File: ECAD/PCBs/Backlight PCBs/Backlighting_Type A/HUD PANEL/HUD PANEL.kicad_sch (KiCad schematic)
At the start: 64 parts, among them J1 Conn_01x04_Female, J2 Conn_01x04_Female

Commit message: Drawing Sheet & Silkscreen update - Backlight Panels (Fc thru Spin)
1:  Updated/Relinked Drawing Sheet for both PCB and Schematics
2:  Standardized Silkscreen (if required)

Finished Remaining Backlighting Type A & Type B PCBs.....
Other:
- title: (none) -> HUD PANEL
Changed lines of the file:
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@@
 (kicad_sch (version 20211123) (generator eeschema)
   (paper "A4")
+  (title_block
+    (title "HUD PANEL")
+    (date "2023-02-10")
+    (rev "3")
+  )
   (junction (at 64.77 133.35) (diameter 0) (color 0 0 0 0)
   )

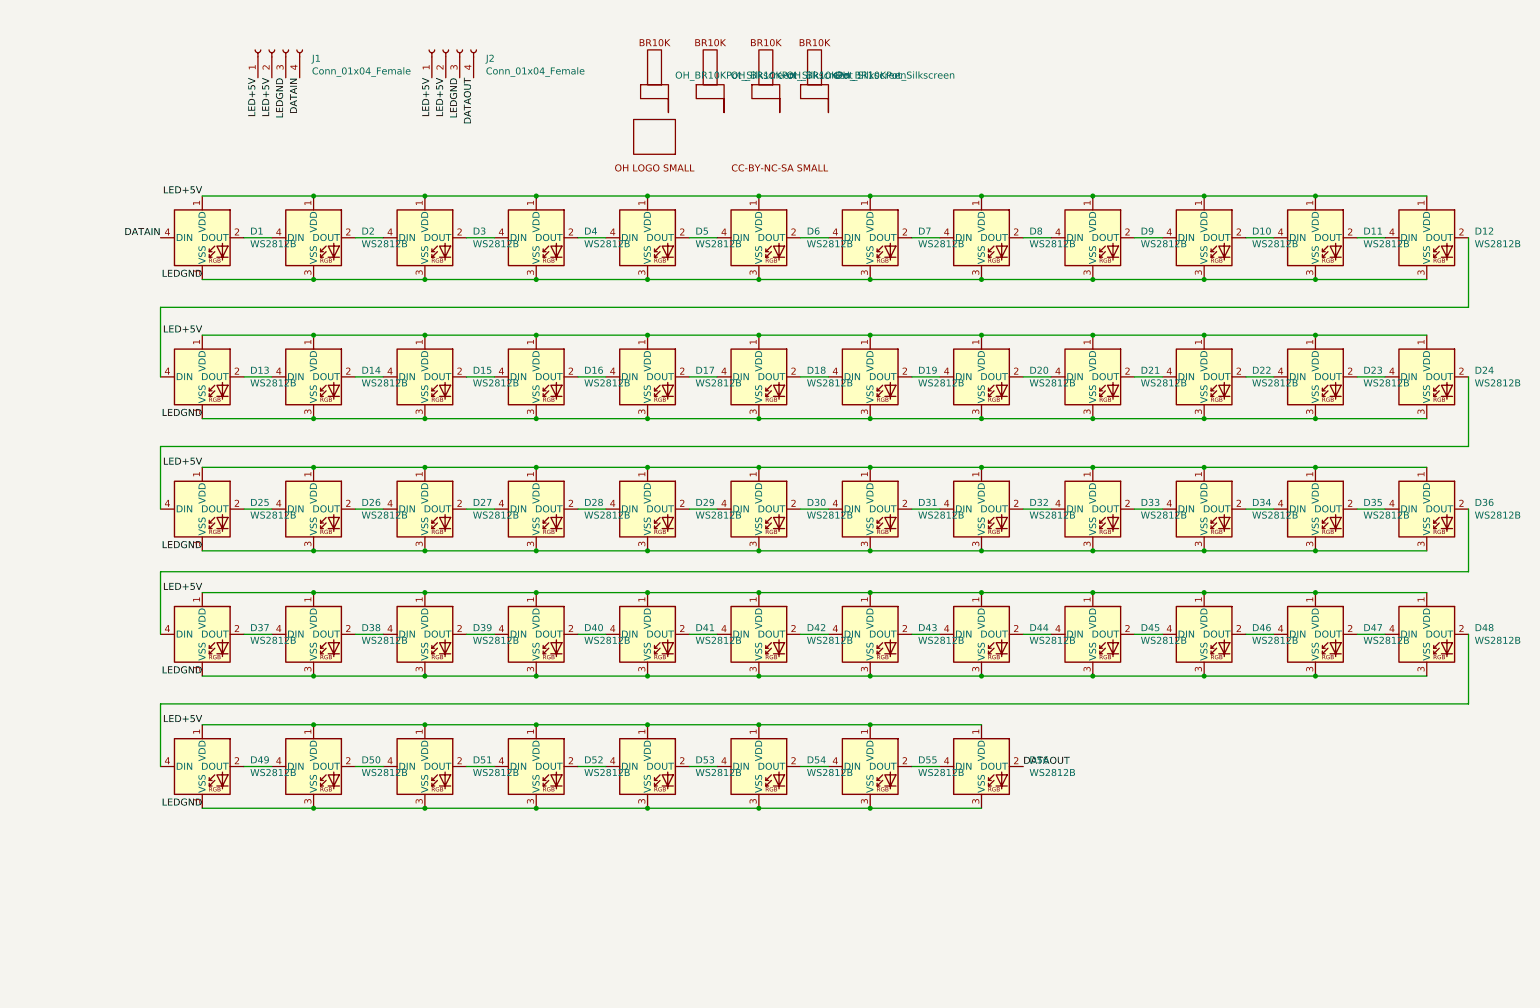
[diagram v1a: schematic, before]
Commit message: KiCad 7 Transition: HUD Panel 100%
HUD Panel 100% ready for release.

Transitioned to K7.
Schematic updated to standard.  DRC complete
PCB board updated with fix for issue #691.  DRC complete
Manufacturing files regenerated.
STEP and PNGs updated.
Footprints/symbols updated.
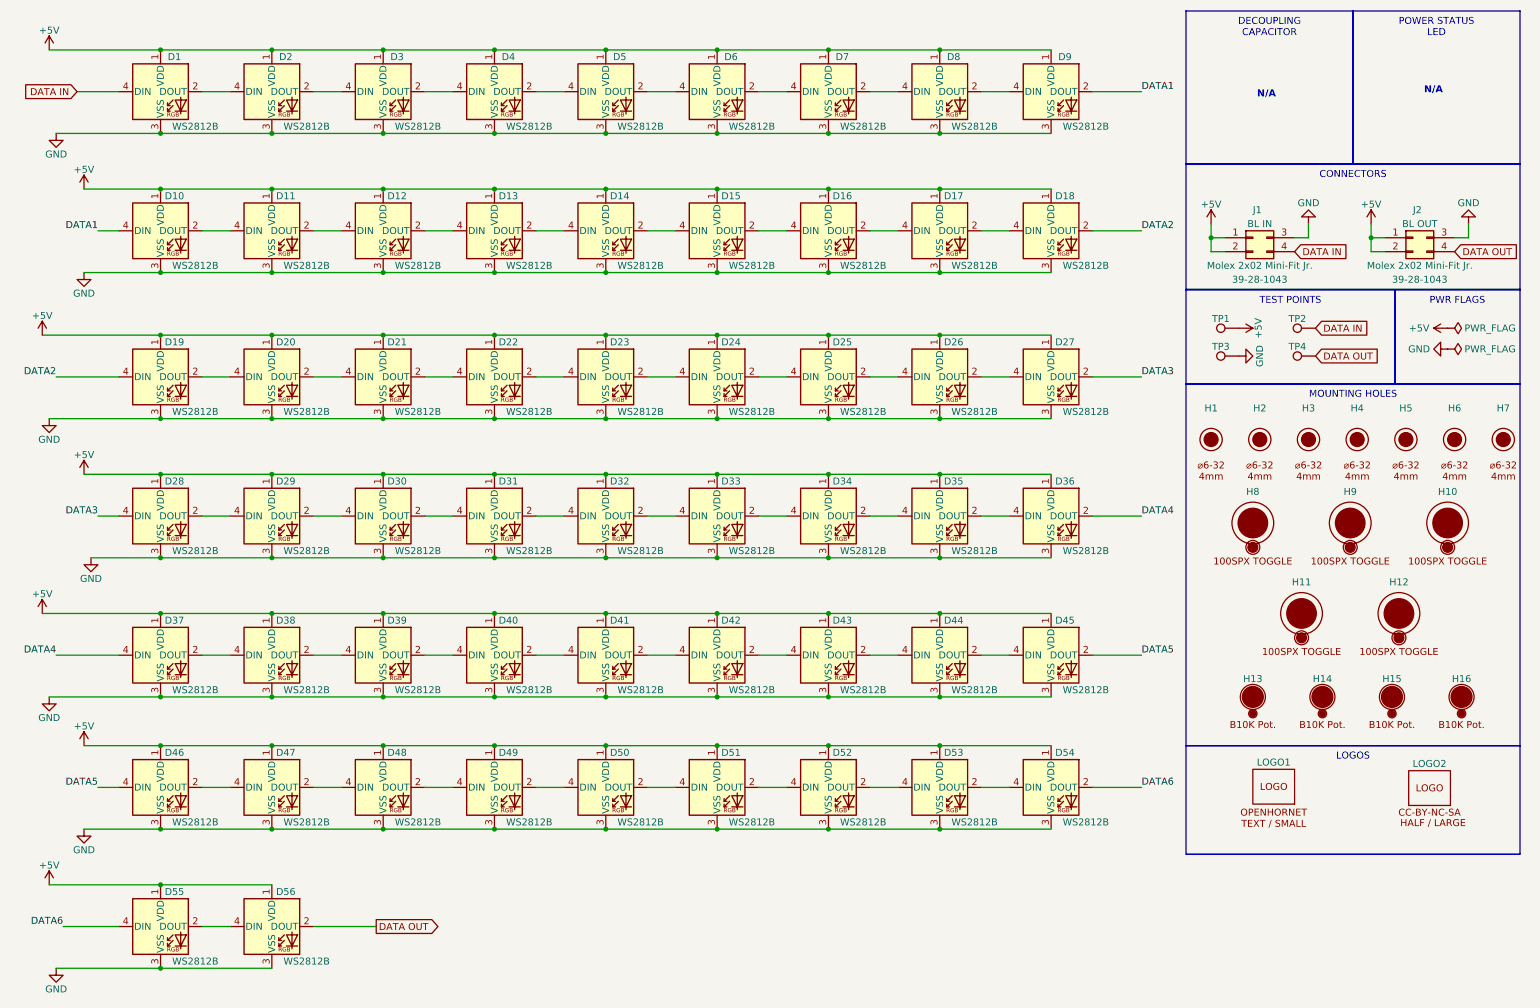
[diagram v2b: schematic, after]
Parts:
- removed J1, J2: Conn_01x04_Female, OH_Footprints:Molex_Mini-Fit_Jr_5566-04A_2x02_P4.20mm_Vertical, symbol Connector:Conn_01x04_Female
- removed LOGO1, LOGO3, LOGO4, LOGO6: OH_BR10KPot_Silkscreen, OH_Footprints:BR10K_Pot_Silkscreen, symbol KiCadCustomLib:OH_BR10KPot_Silkscreen
- added H1, H2, H3, H4, H5, H6, H7: 6x32 / 4mm, OH_Footprints:MountingHole_6-32_PHS, symbol OH_Symbols:MountingHole_6x32_PHS
- added H10, H11, H12, H8, H9: 12.7mm, OH_Footprints:100SPX_Toggle_13mm_x_18mm, symbol OH_Symbols:MountingHole_100SPX_Toggle
- added H13, H14, H15, H16: 11mm, OH_Footprints:BR10K_Pot_11mm_x_11mm, symbol OH_Symbols:MountingHole_B10K_Potentiometer
- added J1, J2: Molex 2x02 Mini-Fit Jr., OH_Footprints:Molex_Mini-Fit_Jr_5566-04A_2x02_P4.20mm_Vertical, symbol OH_Symbols:Molex_2x02_Mini-Fit_Jr.
- added TP1, TP2, TP3, TP4: TestPoint, OH_Footprints:TestPoint_THTPad_D1.5mm_Drill0.7mm, symbol OH_Symbols:TestPoint
- D1, D10, D11, D12, D13, D14, D15, D16, D17, D18, D19, D2, D20, D21, D22, D29, D3, D30, D31, D36, D37, D38, D39, D4, D40, D41, D42, D43, D44, D45, D46, D47, D48, D49, D5, D50, D51, D52, D53, D54, D55, D56, D6, D7, D8, D9: value WS2812B -> RGB; symbol LED:WS2812B -> OH_Symbols:WS2812B; LCSC (none) -> C2761795; Manufacturer PN (none) -> WS2812B
- D23: renamed from D28; value WS2812B -> RGB; symbol LED:WS2812B -> OH_Symbols:WS2812B; LCSC (none) -> C2761795; Manufacturer PN (none) -> WS2812B
- D24: renamed from D23; value WS2812B -> RGB; symbol LED:WS2812B -> OH_Symbols:WS2812B; LCSC (none) -> C2761795; Manufacturer PN (none) -> WS2812B
- D25: renamed from D24; value WS2812B -> RGB; symbol LED:WS2812B -> OH_Symbols:WS2812B; LCSC (none) -> C2761795; Manufacturer PN (none) -> WS2812B
- D26: renamed from D25; value WS2812B -> RGB; symbol LED:WS2812B -> OH_Symbols:WS2812B; LCSC (none) -> C2761795; Manufacturer PN (none) -> WS2812B
- D27: renamed from D26; value WS2812B -> RGB; symbol LED:WS2812B -> OH_Symbols:WS2812B; LCSC (none) -> C2761795; Manufacturer PN (none) -> WS2812B
- D28: renamed from D27; value WS2812B -> RGB; symbol LED:WS2812B -> OH_Symbols:WS2812B; LCSC (none) -> C2761795; Manufacturer PN (none) -> WS2812B
- D32: renamed from D33; value WS2812B -> RGB; symbol LED:WS2812B -> OH_Symbols:WS2812B; LCSC (none) -> C2761795; Manufacturer PN (none) -> WS2812B
- D33: renamed from D32; value WS2812B -> RGB; symbol LED:WS2812B -> OH_Symbols:WS2812B; LCSC (none) -> C2761795; Manufacturer PN (none) -> WS2812B
- D34: renamed from D35; value WS2812B -> RGB; symbol LED:WS2812B -> OH_Symbols:WS2812B; LCSC (none) -> C2761795; Manufacturer PN (none) -> WS2812B
- D35: renamed from D34; value WS2812B -> RGB; symbol LED:WS2812B -> OH_Symbols:WS2812B; LCSC (none) -> C2761795; Manufacturer PN (none) -> WS2812B
- LOGO1: renamed from LOGO2; value OpenHornetLogoSmall -> LOGO; footprint OH_Footprints:OH_LOGO_37.7mm_5.9mm -> OH_Footprints:LOGO_OH_Text_Small; symbol KiCadCustomLib:OpenHornetLogoSmall -> OH_Symbols:LOGO_OpenHornet_Text_Small; now left out of the parts list
- LOGO2: renamed from LOGO5; value CC-BY-NC-SA_Icon -> LOGO; footprint OH_Footprints:CC-BY-NC-SA-Small -> OH_Footprints:LOGO_CC-BY-NC-SA_Half_Large; symbol KiCadCustomLib:CC-BY-NC-SA_Icon -> OH_Symbols:LOGO_License_Half_Large
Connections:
- net DATA1: now reaches D10.4 (DIN), D9.2 (DOUT)
- net DATA2: now reaches D18.2 (DOUT), D19.4 (DIN)
- net at D22.2 (DOUT): now also D23.4 (DIN); no longer D24.4 (DIN)
- net DATA3: now reaches D27.2 (DOUT), D28.4 (DIN)
- net at D28.2 (DOUT): now also D29.4 (DIN); no longer D23.4 (DIN)
- net at D23.2 (DOUT): now also D24.4 (DIN); no longer D29.4 (DIN)
- net at D31.2 (DOUT): now also D32.4 (DIN); no longer D33.4 (DIN)
- net at D33.2 (DOUT): now also D34.4 (DIN); no longer D32.4 (DIN)
- net at D32.2 (DOUT): now also D33.4 (DIN); no longer D35.4 (DIN)
- net at D35.2 (DOUT): now also D36.4 (DIN); no longer D34.4 (DIN)
- net at D34.2 (DOUT): now also D35.4 (DIN); no longer D36.4 (DIN)
- net DATA4: now reaches D36.2 (DOUT), D37.4 (DIN)
- net DATA5: now reaches D45.2 (DOUT), D46.4 (DIN)
- net DATA6: now reaches D54.2 (DOUT), D55.4 (DIN)
- net DATAIN renamed DATA IN
- net DATA IN: now also J1.4 (Pin_4), TP2.1
- net DATAOUT renamed DATA OUT
- net DATA OUT: now also J2.4 (Pin_4), TP4.1
- net LED+5V renamed +5V
- net +5V: now also J1.1 (Pin_1), J1.2 (Pin_3), J2.1 (Pin_1), J2.2 (Pin_3), TP1.1
- net LEDGND renamed GND
- net GND: now also J1.3 (Pin_2), J2.3 (Pin_2), TP3.1
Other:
- note added: "N/A"
- company: (none) -> WWW.OPENHORNET.COM
- moved on the sheet: D1, D10, D11, D12, D13, D14, D15, D16, D17, D18, D19, D2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

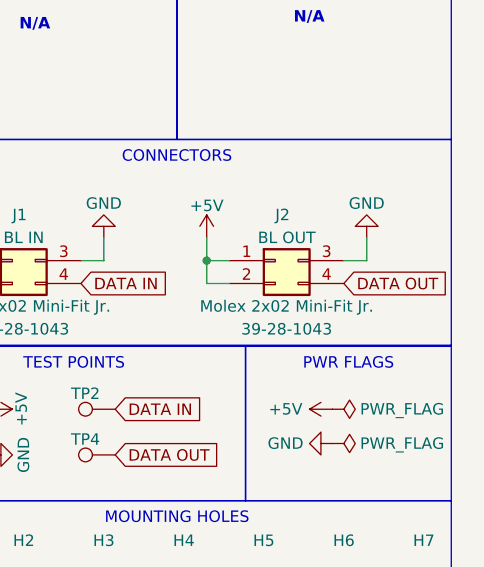
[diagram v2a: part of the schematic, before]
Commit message: KiCad 7 Transition: SELECT JETT PANEL
Transitioned to K7.
Schematic updated to standard.  DRC complete
PCB board updated to fix issue #657 and #646   .  DRC complete
Manufacturing files regenerated.  Consolidated BOMs.
STEP and PNGs updated.
Footprints/symbols updated.

Edited HUD Panel schematic:
- Changed DATA OUTPUT symbol to an actual output symbol instead of an input symbol.
- Changed drawing sheet info - Revision 4.
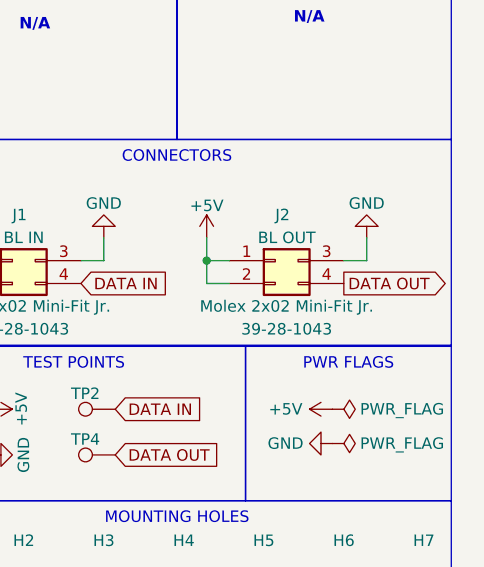
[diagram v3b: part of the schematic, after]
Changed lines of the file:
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@@
     )
   )
-  (global_label "DATA OUT" (shape input) (at 273.05 55.88 0) (fields_autoplaced)
+  (global_label "DATA OUT" (shape output) (at 273.05 55.88 0) (fields_autoplaced)
     (effects (font (size 1.27 1.27)) (justify left))
-    (property "Intersheetrefs" "${INTERSHEET_REFS}" (at 284.9668 55.88 0)
+    (property "Intersheetrefs" "${INTERSHEET_REFS}" (at 284.3126 55.88 0)
       (effects (font (size 1.27 1.27)) (justify left) hide)
     )

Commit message: KiCad 7 Transition: HUD Panel + SEL JETT Update
Updated silkscreen info for mountinghole footprint

KiCad 7 Transition: HUD Panel
HUD Panel 100% ready for release. - Includes fix for conflicting hex nuts.  LEDs rearranged

Transitioned to K7.
Schematic updated to standard.  DRC complete
PCB board updated with fix for issues  #691 and #692 - DRC complete
Manufacturing files regenerated.
STEP and PNGs updated.

SEL JETT Silkscreen - fixed overlapping text
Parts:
- removed D51, D52, D53, D54, D55, D56: RGB, OH_Footprints:LED_WS2812B_PLCC4_5.0x5.0mm_P3.2mm, symbol OH_Symbols:WS2812B
- H1, H2, H3, H4, H5, H6, H7: value 6x32 / 4mm -> #6-32/4mm; now left out of the parts list
- H10, H11, H12, H13, H14, H15, H16, H8, H9: now left out of the parts list
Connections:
- net DATA5 is gone; now on net DATA4: D45.2 (DOUT), D46.4 (DIN)
- net DATA OUT: now also D50.2 (DOUT)
- net DATA1: now also D10.2 (DOUT), D11.4 (DIN); no longer D10.4 (DIN), D9.2 (DOUT)
- net DATA2: now also D22.2 (DOUT), D23.4 (DIN); no longer D18.2 (DOUT), D19.4 (DIN)
- net DATA3: now also D32.2 (DOUT), D33.4 (DIN); no longer D27.2 (DOUT), D28.4 (DIN)
- net DATA4: no longer D36.2 (DOUT), D37.4 (DIN)
- new net: D10.4 (DIN), D9.2 (DOUT)
- new net: D18.2 (DOUT), D19.4 (DIN)
- new net: D27.2 (DOUT), D28.4 (DIN)
- new net: D36.2 (DOUT), D37.4 (DIN)
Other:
- moved on the sheet: D1, D10, D11, D12, D13, D14, D15, D16, D17, D18, D19, D2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
